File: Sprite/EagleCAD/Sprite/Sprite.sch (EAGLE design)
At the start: 24 parts, among them Q1 26MHz, U1 CC430F5137, U2 HMC5883LSMD, U3 ITG-3200

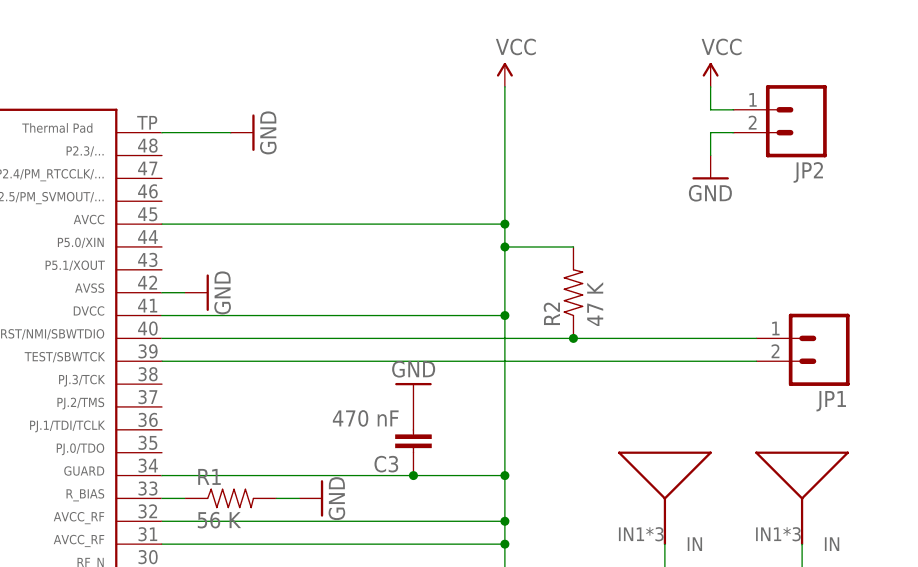
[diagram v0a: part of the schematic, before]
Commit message: Revert "Revert "Removed R2 and changed all passives to 0605 packages""
This reverts commit b3ebe1b95578add26a06b9776380b87bb7788d05.
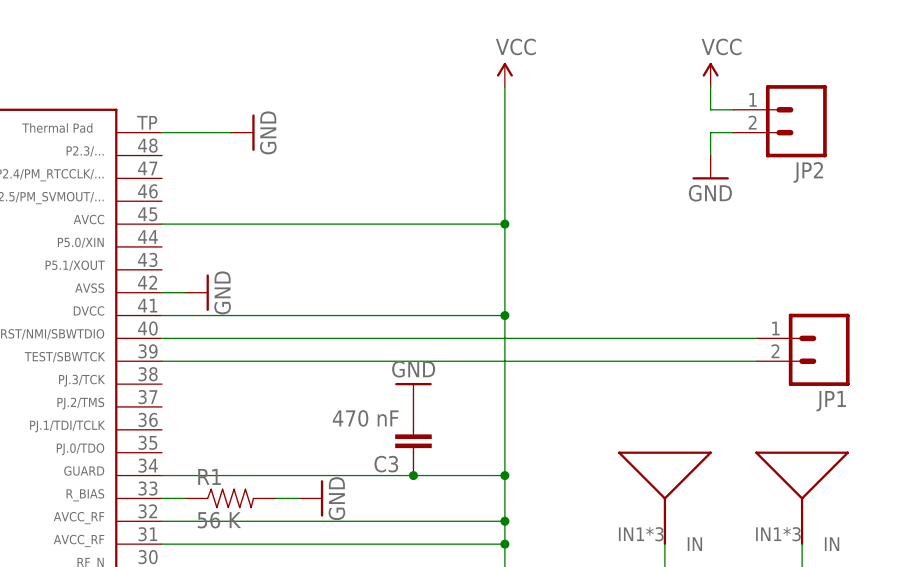
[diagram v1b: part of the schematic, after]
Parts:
- removed R2: 47 K, SparkFun:RESISTOR0603-RES
- C1, C2, C5, C6, C7: device SparkFun:CAP0402-CAP -> SparkFun:CAP0603-CAP
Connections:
- net RST: no longer R2.1
- net VCC: no longer R2.2
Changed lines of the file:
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@@
 <part name="U1" library="TI_MSP430_v16" deviceset="CC430F513X---RGZ48" device="" value="CC430F5137"/>
 <part name="Q1" library="ABM11_JAA" deviceset="ABM11_CERAMIC_SMD_CRYSTAL" device="ABM11" value="26MHz"/>
-<part name="C1" library="SparkFun" deviceset="CAP" device="0402-CAP" value="27 pF"/>
-<part name="C2" library="SparkFun" deviceset="CAP" device="0402-CAP" value="27 pF"/>
+<part name="C1" library="SparkFun" deviceset="CAP" device="0603-CAP" value="27 pF"/>
+<part name="C2" library="SparkFun" deviceset="CAP" device="0603-CAP" value="27 pF"/>
 <part name="R1" library="SparkFun" deviceset="RESISTOR" device="0603-RES" value="56 K"/>
 <part name="C3" library="SparkFun" deviceset="CAP" device="0603-CAP" value="470 nF"/>
 <part name="C4" library="SparkFun" deviceset="CAP" device="0603-CAP" value="470 nF"/>
-<part name="R2" library="SparkFun" deviceset="RESISTOR" device="0603-RES" value="47 K"/>
 <part name="GND3" library="SparkFun" deviceset="GND" device=""/>
 <part name="GND4" library="SparkFun" deviceset="GND" device=""/>
@@
 <part name="P+2" library="SparkFun" deviceset="VCC" device=""/>
 <part name="U2" library="SparkFun" deviceset="HMC5883L" device="SMD"/>
-<part name="C5" library="SparkFun" deviceset="CAP" device="0402-CAP" value=".1uF"/>
-<part name="C6" library="SparkFun" deviceset="CAP" device="0402-CAP" value=".22uF"/>
-<part name="C7" library="SparkFun" deviceset="CAP" device="0402-CAP" value="4.7uF"/>
+<part name="C5" library="SparkFun" deviceset="CAP" device="0603-CAP" value=".1uF"/>
+<part name="C6" library="SparkFun" deviceset="CAP" device="0603-CAP" value=".22uF"/>
+<part name="C7" library="SparkFun" deviceset="CAP" device="0603-CAP" value="4.7uF"/>
 <part name="GND11" library="SparkFun" deviceset="GND" device=""/>
 <part name="GND12" library="SparkFun" deviceset="GND" device=""/>
@@
 <instance part="C3" gate="G$1" x="203.2" y="83.82" rot="R180"/>
 <instance part="C4" gate="G$1" x="124.46" y="99.06" rot="R270"/>
-<instance part="R2" gate="G$1" x="220.98" y="99.06" rot="R90"/>
 <instance part="GND3" gate="1" x="180.34" y="99.06" rot="R90"/>
 <instance part="GND4" gate="1" x="185.42" y="116.84" rot="R90"/>
@@
 <wire x1="175.26" y1="63.5" x2="213.36" y2="63.5" width="0.1524" layer="91"/>
 <wire x1="175.26" y1="106.68" x2="213.36" y2="106.68" width="0.1524" layer="91"/>
-<wire x1="213.36" y1="106.68" x2="213.36" y2="104.14" width="0.1524" layer="91"/>
-<wire x1="213.36" y1="104.14" x2="213.36" y2="96.52" width="0.1524" layer="91"/>
+<wire x1="213.36" y1="106.68" x2="213.36" y2="96.52" width="0.1524" layer="91"/>
 <wire x1="175.26" y1="96.52" x2="213.36" y2="96.52" width="0.1524" layer="91"/>
 <wire x1="213.36" y1="96.52" x2="213.36" y2="78.74" width="0.1524" layer="91"/>
@@
 <wire x1="213.36" y1="71.12" x2="213.36" y2="63.5" width="0.1524" layer="91"/>
 <wire x1="175.26" y1="71.12" x2="213.36" y2="71.12" width="0.1524" layer="91"/>
-<wire x1="220.98" y1="104.14" x2="213.36" y2="104.14" width="0.1524" layer="91"/>
 <junction x="116.84" y="60.96"/>
 <junction x="213.36" y="60.96"/>
@@
 <junction x="213.36" y="73.66"/>
 <junction x="213.36" y="71.12"/>
-<junction x="213.36" y="104.14"/>
 <pinref part="U1" gate="G$1" pin="27"/>
 <pinref part="U1" gate="G$1" pin="22"/>
@@
 <pinref part="U1" gate="G$1" pin="32"/>
 <pinref part="U1" gate="G$1" pin="31"/>
-<pinref part="R2" gate="G$1" pin="2"/>
 <pinref part="P+2" gate="1" pin="VCC"/>
 <wire x1="213.36" y1="121.92" x2="213.36" y2="106.68" width="0.1524" layer="91"/>
@@
 <net name="RST" class="0">
 <segment>
-<wire x1="175.26" y1="93.98" x2="220.98" y2="93.98" width="0.1524" layer="91"/>
-<wire x1="220.98" y1="93.98" x2="241.3" y2="93.98" width="0.1524" layer="91"/>
+<wire x1="175.26" y1="93.98" x2="241.3" y2="93.98" width="0.1524" layer="91"/>
 <pinref part="U1" gate="G$1" pin="40"/>
-<pinref part="R2" gate="G$1" pin="1"/>
 <pinref part="JP1" gate="G$1" pin="1"/>
-<junction x="220.98" y="93.98"/>
-</segment>
-</net>
+</segment>
+</net>

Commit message: Revert "Removed R2 and changed all passives to 0605 packages"
This reverts commit fe0fb0a19ac4f8aff1bc8119a0abeef84ddcba56.
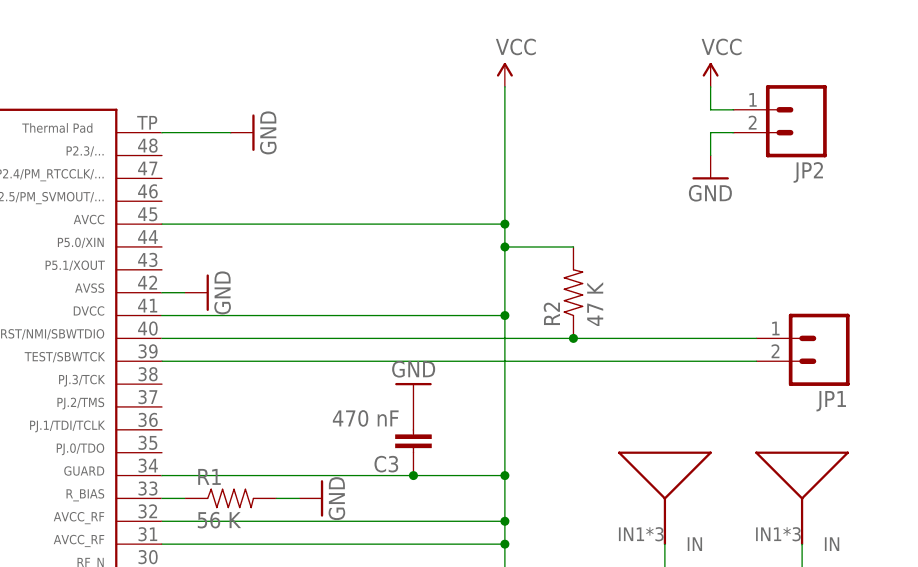
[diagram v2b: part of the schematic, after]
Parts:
- added R2: 47 K, SparkFun:RESISTOR0603-RES
- C1, C2, C5, C6, C7: device SparkFun:CAP0603-CAP -> SparkFun:CAP0402-CAP
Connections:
- net RST: now also R2.1
- net VCC: now also R2.2
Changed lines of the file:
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@@
 <part name="U1" library="TI_MSP430_v16" deviceset="CC430F513X---RGZ48" device="" value="CC430F5137"/>
 <part name="Q1" library="ABM11_JAA" deviceset="ABM11_CERAMIC_SMD_CRYSTAL" device="ABM11" value="26MHz"/>
-<part name="C1" library="SparkFun" deviceset="CAP" device="0603-CAP" value="27 pF"/>
-<part name="C2" library="SparkFun" deviceset="CAP" device="0603-CAP" value="27 pF"/>
+<part name="C1" library="SparkFun" deviceset="CAP" device="0402-CAP" value="27 pF"/>
+<part name="C2" library="SparkFun" deviceset="CAP" device="0402-CAP" value="27 pF"/>
 <part name="R1" library="SparkFun" deviceset="RESISTOR" device="0603-RES" value="56 K"/>
 <part name="C3" library="SparkFun" deviceset="CAP" device="0603-CAP" value="470 nF"/>
 <part name="C4" library="SparkFun" deviceset="CAP" device="0603-CAP" value="470 nF"/>
+<part name="R2" library="SparkFun" deviceset="RESISTOR" device="0603-RES" value="47 K"/>
 <part name="GND3" library="SparkFun" deviceset="GND" device=""/>
 <part name="GND4" library="SparkFun" deviceset="GND" device=""/>
@@
 <part name="P+2" library="SparkFun" deviceset="VCC" device=""/>
 <part name="U2" library="SparkFun" deviceset="HMC5883L" device="SMD"/>
-<part name="C5" library="SparkFun" deviceset="CAP" device="0603-CAP" value=".1uF"/>
-<part name="C6" library="SparkFun" deviceset="CAP" device="0603-CAP" value=".22uF"/>
-<part name="C7" library="SparkFun" deviceset="CAP" device="0603-CAP" value="4.7uF"/>
+<part name="C5" library="SparkFun" deviceset="CAP" device="0402-CAP" value=".1uF"/>
+<part name="C6" library="SparkFun" deviceset="CAP" device="0402-CAP" value=".22uF"/>
+<part name="C7" library="SparkFun" deviceset="CAP" device="0402-CAP" value="4.7uF"/>
 <part name="GND11" library="SparkFun" deviceset="GND" device=""/>
 <part name="GND12" library="SparkFun" deviceset="GND" device=""/>
@@
 <instance part="C3" gate="G$1" x="203.2" y="83.82" rot="R180"/>
 <instance part="C4" gate="G$1" x="124.46" y="99.06" rot="R270"/>
+<instance part="R2" gate="G$1" x="220.98" y="99.06" rot="R90"/>
 <instance part="GND3" gate="1" x="180.34" y="99.06" rot="R90"/>
 <instance part="GND4" gate="1" x="185.42" y="116.84" rot="R90"/>
@@
 <wire x1="175.26" y1="63.5" x2="213.36" y2="63.5" width="0.1524" layer="91"/>
 <wire x1="175.26" y1="106.68" x2="213.36" y2="106.68" width="0.1524" layer="91"/>
-<wire x1="213.36" y1="106.68" x2="213.36" y2="96.52" width="0.1524" layer="91"/>
+<wire x1="213.36" y1="106.68" x2="213.36" y2="104.14" width="0.1524" layer="91"/>
+<wire x1="213.36" y1="104.14" x2="213.36" y2="96.52" width="0.1524" layer="91"/>
 <wire x1="175.26" y1="96.52" x2="213.36" y2="96.52" width="0.1524" layer="91"/>
 <wire x1="213.36" y1="96.52" x2="213.36" y2="78.74" width="0.1524" layer="91"/>
@@
 <wire x1="213.36" y1="71.12" x2="213.36" y2="63.5" width="0.1524" layer="91"/>
 <wire x1="175.26" y1="71.12" x2="213.36" y2="71.12" width="0.1524" layer="91"/>
+<wire x1="220.98" y1="104.14" x2="213.36" y2="104.14" width="0.1524" layer="91"/>
 <junction x="116.84" y="60.96"/>
 <junction x="213.36" y="60.96"/>
@@
 <junction x="213.36" y="73.66"/>
 <junction x="213.36" y="71.12"/>
+<junction x="213.36" y="104.14"/>
 <pinref part="U1" gate="G$1" pin="27"/>
 <pinref part="U1" gate="G$1" pin="22"/>
@@
 <pinref part="U1" gate="G$1" pin="32"/>
 <pinref part="U1" gate="G$1" pin="31"/>
+<pinref part="R2" gate="G$1" pin="2"/>
 <pinref part="P+2" gate="1" pin="VCC"/>
 <wire x1="213.36" y1="121.92" x2="213.36" y2="106.68" width="0.1524" layer="91"/>
@@
 <net name="RST" class="0">
 <segment>
-<wire x1="175.26" y1="93.98" x2="241.3" y2="93.98" width="0.1524" layer="91"/>
+<wire x1="175.26" y1="93.98" x2="220.98" y2="93.98" width="0.1524" layer="91"/>
+<wire x1="220.98" y1="93.98" x2="241.3" y2="93.98" width="0.1524" layer="91"/>
 <pinref part="U1" gate="G$1" pin="40"/>
+<pinref part="R2" gate="G$1" pin="1"/>
 <pinref part="JP1" gate="G$1" pin="1"/>
-</segment>
-</net>
+<junction x="220.98" y="93.98"/>
+</segment>
+</net>
